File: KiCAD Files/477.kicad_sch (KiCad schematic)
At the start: 28 parts, among them IC1 W25N01GVSFIG, IC2 W25N01GVSFIG, IC3 W25N01GVSFIG, IC4 W25N01GVSFIG, IC6 USBLC6-2SC6, J1 BM06B-SRSS-TBT_LF__SN_, J2 6364372-2, J5 BM07B-SRSS-TB_LF__SN_, J6 BM09B-SRSS-TB_LF__SN_

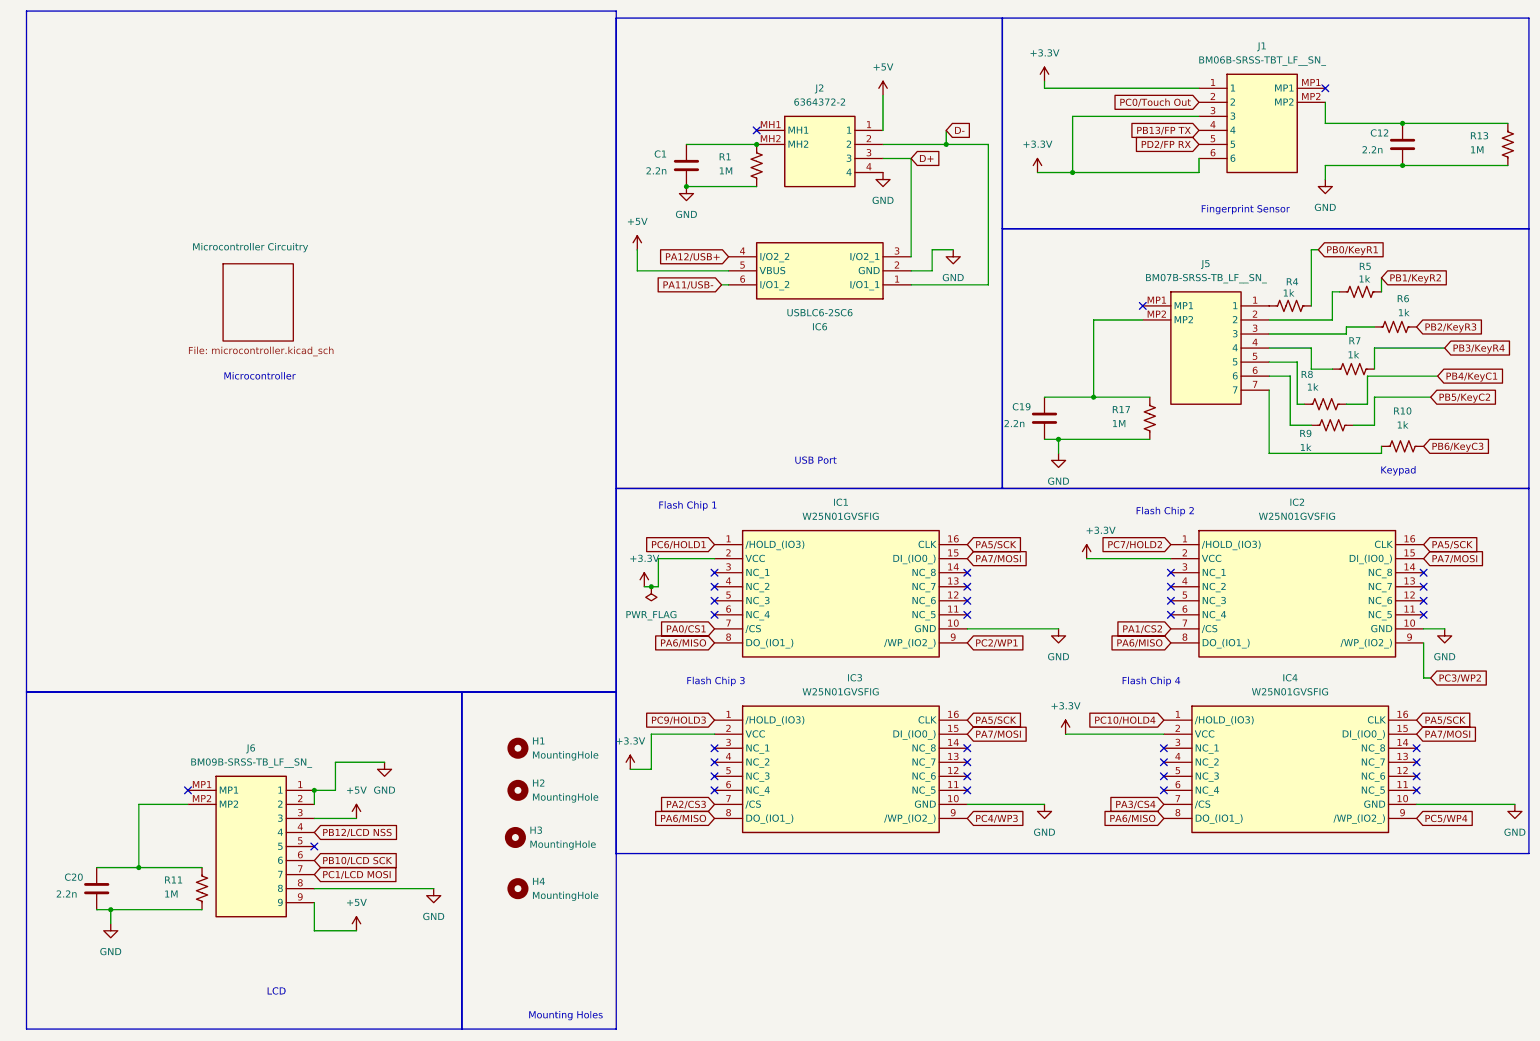
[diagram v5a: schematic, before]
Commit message: added testing points
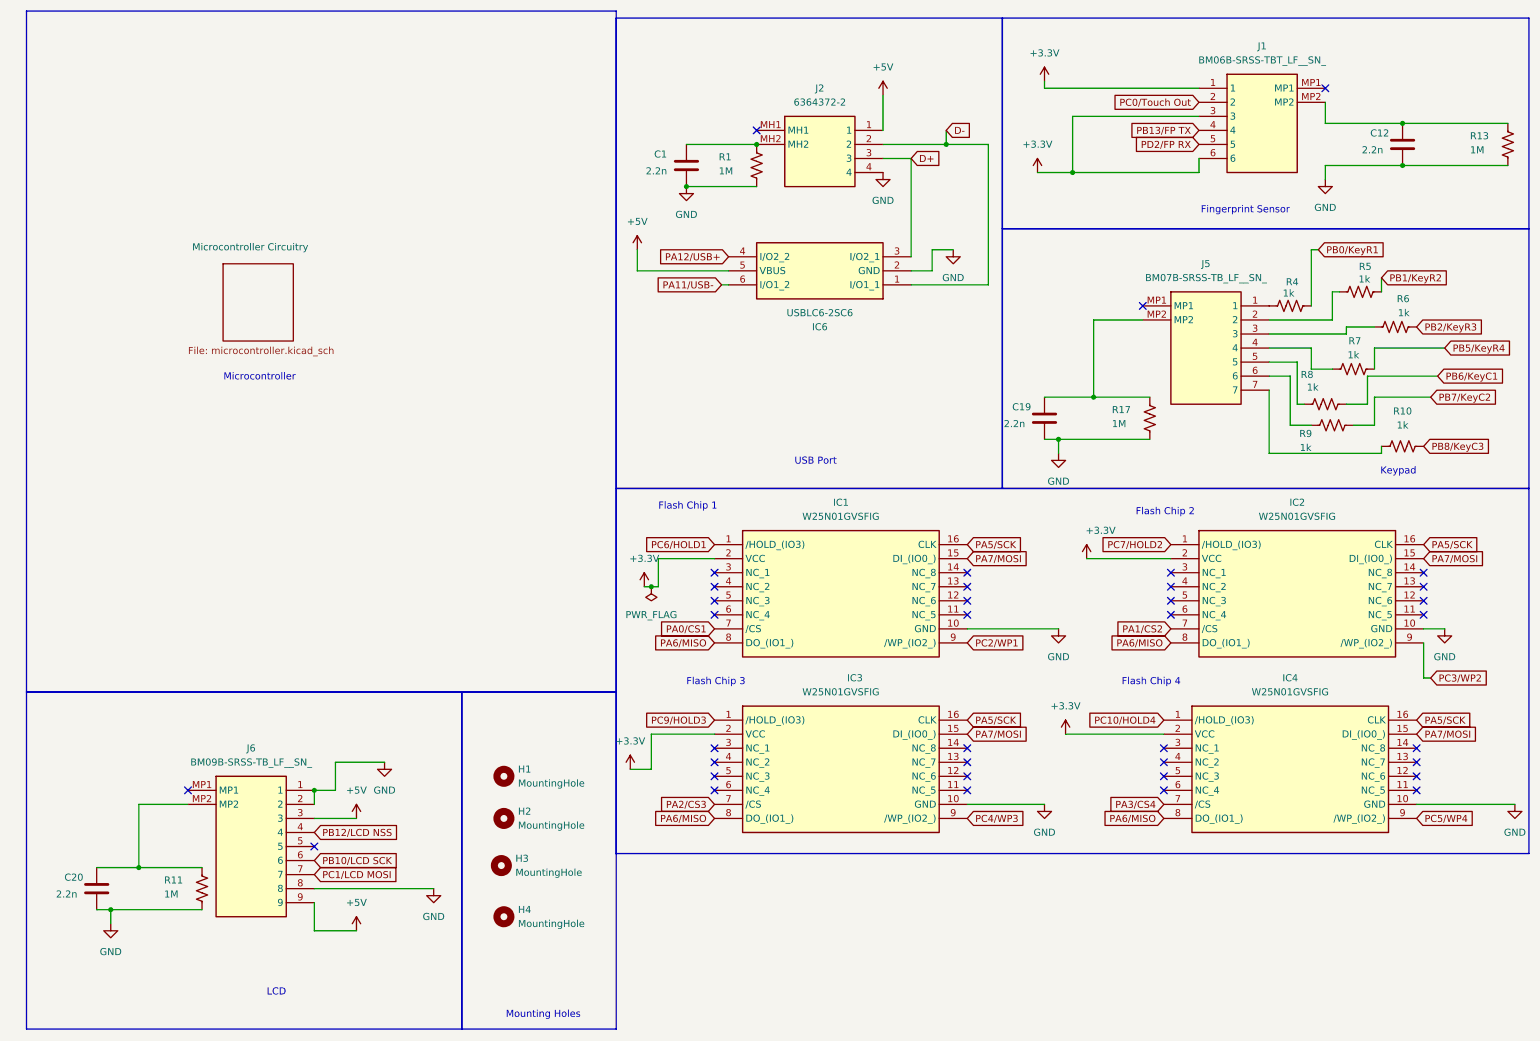
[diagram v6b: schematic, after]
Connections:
- net PB3/KeyR4 renamed PB5/KeyR4
- net PB4/KeyC1 renamed PB6/KeyC1
- net PB5/KeyC2 renamed PB7/KeyC2
- net PB6/KeyC3 renamed PB8/KeyC3
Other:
- moved on the sheet: H1, H2, H3, H4
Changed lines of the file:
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@@
 	(text "Mounting Holes\n"
 		(exclude_from_sim no)
-		(at 110.236 194.564 0)
+		(at 106.172 194.31 0)
 		(effects
 			(font
@@
 		)
 	)
-	(global_label "PB3{slash}KeyR4"
+	(global_label "PB5{slash}KeyR4"
 		(shape input)
 		(at 269.24 73.66 0)
@@
 		)
 	)
-	(global_label "PB4{slash}KeyC1"
+	(global_label "PB6{slash}KeyC1"
 		(shape input)
 		(at 267.97 78.74 0)
@@
 		)
 	)
-	(global_label "PB6{slash}KeyC3"
+	(global_label "PB8{slash}KeyC3"
 		(shape input)
 		(at 265.43 91.44 0)
@@
 		)
 	)
-	(global_label "PB5{slash}KeyC2"
+	(global_label "PB7{slash}KeyC2"
 		(shape input)
 		(at 266.7 82.55 0)
@@
 	(symbol
 		(lib_id "Mechanical:MountingHole")
-		(at 101.6 146.05 0)
+		(at 99.06 151.13 0)
 		(unit 1)
 		(exclude_from_sim yes)
@@
 		(fields_autoplaced yes)
 		(property "Reference" "H1"
-			(at 104.14 144.7799 0)
+			(at 101.6 149.8599 0)
 			(effects
 				(font
@@
 		)
 		(property "Value" "MountingHole"
-			(at 104.14 147.3199 0)
+			(at 101.6 152.3999 0)
 			(effects
 				(font
@@
 		)
 		(property "Footprint" "MountingHole:MountingHole_3.2mm_M3_DIN965"
-			(at 101.6 146.05 0)
+			(at 99.06 151.13 0)
 			(effects
 				(font
@@
 		)
 		(property "Datasheet" "~"
-			(at 101.6 146.05 0)
+			(at 99.06 151.13 0)
 			(effects
 				(font
@@
 		)
 		(property "Description" "Mounting Hole without connection"
-			(at 101.6 146.05 0)
+			(at 99.06 151.13 0)
 			(effects
 				(font
@@
 	(symbol
 		(lib_id "Mechanical:MountingHole")
-		(at 101.6 153.67 0)
+		(at 99.06 158.75 0)
 		(unit 1)
 		(exclude_from_sim yes)
@@
 		(fields_autoplaced yes)
 		(property "Reference" "H2"
-			(at 104.14 152.3999 0)
+			(at 101.6 157.4799 0)
 			(effects
 				(font
@@
 		)
 		(property "Value" "MountingHole"
-			(at 104.14 154.9399 0)
+			(at 101.6 160.0199 0)
 			(effects
 				(font
@@
 		)
 		(property "Footprint" "MountingHole:MountingHole_3.2mm_M3_DIN965"
-			(at 101.6 153.67 0)
+			(at 99.06 158.75 0)
 			(effects
 				(font
@@
 		)
 		(property "Datasheet" "~"
-			(at 101.6 153.67 0)
+			(at 99.06 158.75 0)
 			(effects
 				(font
@@
 		)
 		(property "Description" "Mounting Hole without connection"
-			(at 101.6 153.67 0)
+			(at 99.06 158.75 0)
 			(effects
 				(font
@@
 	(symbol
 		(lib_id "Mechanical:MountingHole")
-		(at 101.6 171.45 0)
+		(at 99.06 176.53 0)
 		(unit 1)
 		(exclude_from_sim yes)
@@
 		(fields_autoplaced yes)
 		(property "Reference" "H4"
-			(at 104.14 170.1799 0)
+			(at 101.6 175.2599 0)
 			(effects
 				(font
@@
 		)
 		(property "Value" "MountingHole"
-			(at 104.14 172.7199 0)
+			(at 101.6 177.7999 0)
 			(effects
 				(font
@@
 		)
 		(property "Footprint" "MountingHole:MountingHole_3.2mm_M3_DIN965"
-			(at 101.6 171.45 0)
+			(at 99.06 176.53 0)
 			(effects
 				(font
@@
 		)
 		(property "Datasheet" "~"
-			(at 101.6 171.45 0)
+			(at 99.06 176.53 0)
 			(effects
 				(font
@@
 		)
 		(property "Description" "Mounting Hole without connection"
-			(at 101.6 171.45 0)
+			(at 99.06 176.53 0)
 			(effects
 				(font
@@
 	(symbol
 		(lib_id "Mechanical:MountingHole")
-		(at 101.1393 162.1952 0)
+		(at 98.5993 167.2752 0)
 		(unit 1)
 		(exclude_from_sim yes)
@@
 		(fields_autoplaced yes)
 		(property "Reference" "H3"
-			(at 103.6793 160.9251 0)
+			(at 101.1393 166.0051 0)
 			(effects
 				(font
@@
 		)
 		(property "Value" "MountingHole"
-			(at 103.6793 163.4651 0)
+			(at 101.1393 168.5451 0)
 			(effects
 				(font
@@
 		)
 		(property "Footprint" "MountingHole:MountingHole_3.2mm_M3_DIN965"
-			(at 101.1393 162.1952 0)
+			(at 98.5993 167.2752 0)
 			(effects
 				(font
@@
 		)
 		(property "Datasheet" "~"
-			(at 101.1393 162.1952 0)
+			(at 98.5993 167.2752 0)
 			(effects
 				(font
@@
 		)
 		(property "Description" "Mounting Hole without connection"
-			(at 101.1393 162.1952 0)
+			(at 98.5993 167.2752 0)
 			(effects
 				(font

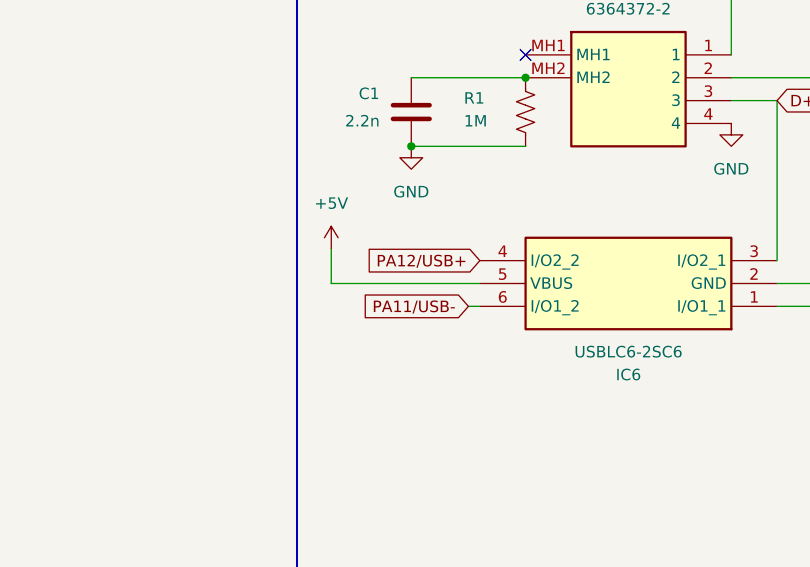
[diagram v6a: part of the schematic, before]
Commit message: routed essential signals
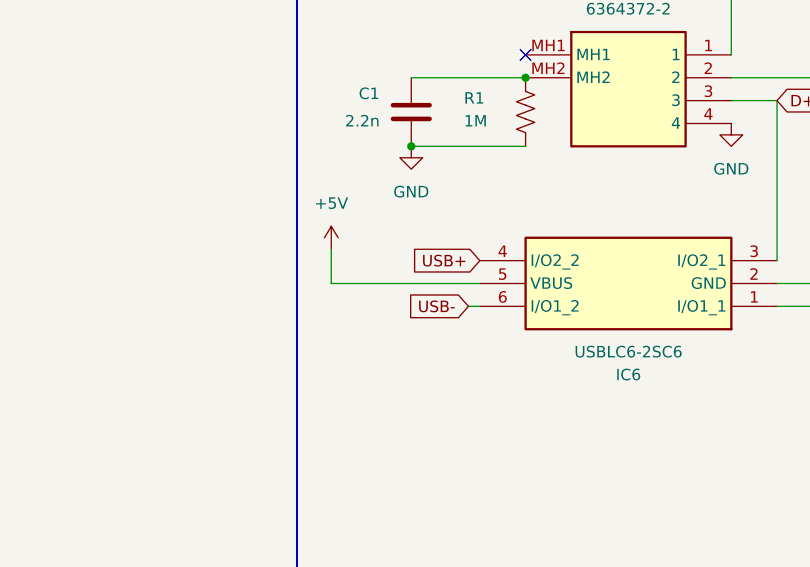
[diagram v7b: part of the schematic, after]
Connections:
- net PA11/USB- renamed USB-
- net PA12/USB+ renamed USB+
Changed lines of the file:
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@@
 		)
 	)
-	(global_label "PA11{slash}USB-"
+	(global_label "USB-"
 		(shape input)
 		(at 138.43 62.23 180)
@@
 		)
 		(property "Intersheetrefs" "${INTERSHEET_REFS}"
-			(at 123.9543 62.23 0)
+			(at 130.0624 62.23 0)
 			(effects
 				(font
@@
 		)
 	)
-	(global_label "PA12{slash}USB+"
+	(global_label "USB+"
 		(shape input)
 		(at 139.7 57.15 180)
@@
 		)
 		(property "Intersheetrefs" "${INTERSHEET_REFS}"
-			(at 125.2243 57.15 0)
-			(effects
-				(font
+			(at 131.3324 57.15 0)
+			(effects
+				(font

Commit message: finished file
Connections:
- net PA0/CS1 renamed PC9/CS1
- net PA1/CS2 renamed PC10/CS2
- net PA2/CS3 renamed PA3/CS3
- net PA3/CS4 renamed PA1/CS4
- net PC10/HOLD4 renamed PA2/HOLD4
- net PC2/WP1 renamed PC7/WP1
- net PC4/WP3 renamed PC5/WP3
- net PC5/WP4 renamed PA0/WP4
- net PC7/HOLD2 renamed PC2/HOLD2
- net PC9/HOLD3 renamed PC4/HOLD3
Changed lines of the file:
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@@
 		)
 	)
-	(global_label "PC5{slash}WP4"
+	(global_label "PA0{slash}WP4"
 		(shape input)
 		(at 264.16 158.75 0)
@@
 		)
 		(property "Intersheetrefs" "${INTERSHEET_REFS}"
-			(at 276.1561 158.75 0)
-			(effects
-				(font
-					(size 1.27 1.27)
-				)
-				(justify left)
-				(hide yes)
-			)
-		)
-	)
-	(global_label "PA0{slash}CS1"
+			(at 275.9747 158.75 0)
+			(effects
+				(font
+					(size 1.27 1.27)
+				)
+				(justify left)
+				(hide yes)
+			)
+		)
+	)
+	(global_label "PC9{slash}CS1"
 		(shape input)
 		(at 137.16 124.46 180)
@@
 		)
 		(property "Intersheetrefs" "${INTERSHEET_REFS}"
-			(at 125.5872 124.46 0)
+			(at 125.4058 124.46 0)
 			(effects
 				(font
@@
 		)
 	)
-	(global_label "PC10{slash}HOLD4"
+	(global_label "PA2{slash}HOLD4"
 		(shape input)
 		(at 218.44 140.97 180)
@@
 		)
 		(property "Intersheetrefs" "${INTERSHEET_REFS}"
-			(at 202.9967 140.97 0)
+			(at 204.3876 140.97 0)
 			(effects
 				(font
@@
 		)
 	)
-	(global_label "PC7{slash}HOLD2"
+	(global_label "PC2{slash}HOLD2"
 		(shape input)
 		(at 219.71 109.22 180)
@@
 		)
 	)
-	(global_label "PA2{slash}CS3"
+	(global_label "PA3{slash}CS3"
 		(shape input)
 		(at 137.16 156.21 180)
@@
 		)
 	)
-	(global_label "PA1{slash}CS2"
+	(global_label "PC10{slash}CS2"
 		(shape input)
 		(at 219.71 124.46 180)
@@
 		)
 		(property "Intersheetrefs" "${INTERSHEET_REFS}"
-			(at 208.1372 124.46 0)
-			(effects
-				(font
-					(size 1.27 1.27)
-				)
-				(justify right)
-				(hide yes)
-			)
-		)
-	)
-	(global_label "PC2{slash}WP1"
+			(at 206.7463 124.46 0)
+			(effects
+				(font
+					(size 1.27 1.27)
+				)
+				(justify right)
+				(hide yes)
+			)
+		)
+	)
+	(global_label "PC7{slash}WP1"
 		(shape input)
 		(at 182.88 127 0)
@@
 		)
 	)
-	(global_label "PC9{slash}HOLD3"
+	(global_label "PC4{slash}HOLD3"
 		(shape input)
 		(at 137.16 140.97 180)
@@
 		)
 	)
-	(global_label "PA3{slash}CS4"
+	(global_label "PA1{slash}CS4"
 		(shape input)
 		(at 218.44 156.21 180)
@@
 		)
 	)
-	(global_label "PC4{slash}WP3"
+	(global_label "PC5{slash}WP3"
 		(shape input)
 		(at 182.88 158.75 0)
